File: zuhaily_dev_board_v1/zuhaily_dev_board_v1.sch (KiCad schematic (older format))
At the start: 56 parts, among them J1 USB_B_Micro, J2 Micro_SD_Card, J3 DC_JACK, J4 Conn_01x32_Female, Q1 FS8205A, Q2 FDN340P, SW1 SW_DPDT_x2, SW2 SW_SPST, SW3 SW_DIP_x04, SW4 SW_DIP_x04, SW5 SW_DIP_x04, U1 74LVC245, U10 DW-01, U2 LM1117-5.0, U3 CH340G, U4 LM1117-3.3, U5 ATmega328-PU, U7 TP4056, U8 LMV358, Y1 Crystal_12MHz, Y2 Crystal_16MHz

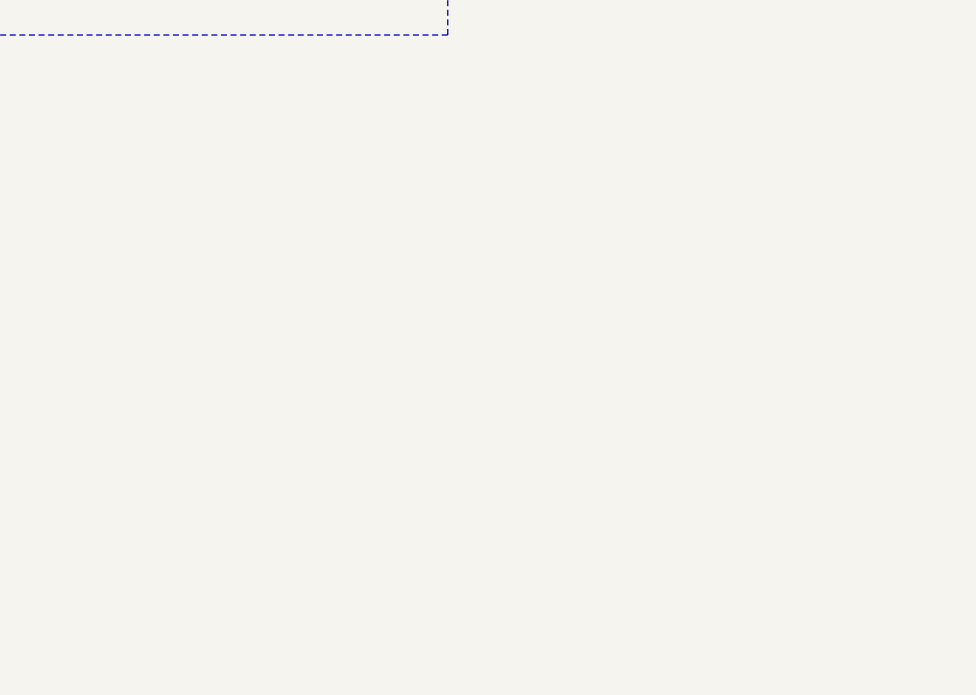
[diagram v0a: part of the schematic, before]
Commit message: added rtc
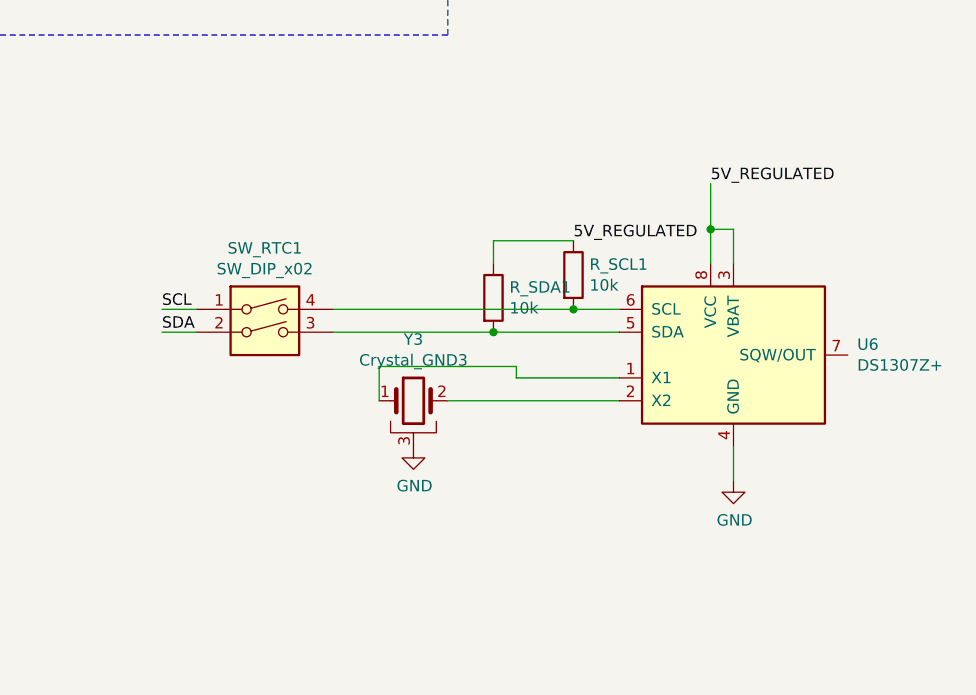
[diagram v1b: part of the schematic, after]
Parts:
- added R_SCL1, R_SDA1: 10k, Resistor_THT:R_Axial_DIN0207_L6.3mm_D2.5mm_P7.62mm_Horizontal, symbol Device:R
- added SW_RTC1: SW_DIP_x02, Button_Switch_THT:SW_DIP_SPSTx02_Slide_9.78x7.26mm_W7.62mm_P2.54mm, symbol Switch:SW_DIP_x02
- added U6: DS1307Z+, Package_SO:SOIC-8_3.9x4.9mm_P1.27mm, symbol Timer_RTC:DS1307Z+
- added Y3: Crystal_GND3, Crystal:Crystal_AT310_D3.0mm_L10.0mm_Horizontal_1EP_style1, symbol Device:Crystal_GND3
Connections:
- net 5V_FILTERED: now also R_SCL1.1, R_SDA1.1, U6.3 (VBAT), U6.8 (VCC)
- net GND: now also U6.4 (GND), Y3.3
- net PC_4: now also SW_RTC1.2
- net PC_5: now also SW_RTC1.1
- new net: U6.1 (X1), Y3.1
- new net: U6.2 (X2), Y3.2
- new net: R_SDA1.2, SW_RTC1.3, U6.5 (SDA)
- new net: R_SCL1.2, SW_RTC1.4, U6.6 (SCL)
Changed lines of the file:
@@
 Wire Wire Line
 	10700 7750 11300 7750
+$Comp
+L Timer_RTC:DS1307Z+ U6
+U 1 1 5C5C03AE
+P 23100 6600
+F 0 "U6" H 23641 6646 50  0000 L CNN
+F 1 "DS1307Z+" H 23641 6555 50  0000 L CNN
+F 2 "Package_SO:SOIC-8_3.9x4.9mm_P1.27mm" H 23100 6100 50  0001 C CNN
+F 3 "https://datasheets.maximintegrated.com/en/ds/DS1307.pdf" H 23100 6600 50  0001 C CNN
+	1    23100 6600
+	1    0    0    -1
+$EndComp
+Text Label 20600 6500 0    50   ~ 0
+SDA
+Text Label 20600 6400 0    50   ~ 0
+SCL
+Text Label 23000 5850 0    50   ~ 0
+5V_REGULATED
+Wire Wire Line
+	23000 6200 23000 6050
+Wire Wire Line
+	23100 6200 23100 6050
+Wire Wire Line
+	23100 6050 23000 6050
+Connection ~ 23000 6050
+Wire Wire Line
+	23000 6050 23000 5850
+Wire Wire Line
+	22600 6700 22150 6700
+Wire Wire Line
+	22150 6700 22150 6650
+$Comp
+L power:GND #PWR0127
+U 1 1 5C665D4A
+P 23100 7150
+F 0 "#PWR0127" H 23100 6900 50  0001 C CNN
+F 1 "GND" H 23105 6977 50  0000 C CNN
+F 2 "" H 23100 7150 50  0001 C CNN
+F 3 "" H 23100 7150 50  0001 C CNN
+	1    23100 7150
+	1    0    0    -1
+$EndComp
+Wire Wire Line
+	23100 7150 23100 7000
+$Comp
+L Device:R R_SCL1
+U 1 1 5C682EB7
+P 22400 6250
+F 0 "R_SCL1" H 22470 6296 50  0000 L CNN
+F 1 "10k" H 22470 6205 50  0000 L CNN
+F 2 "Resistor_THT:R_Axial_DIN0207_L6.3mm_D2.5mm_P7.62mm_Horizontal" V 22330 6250 50  0001 C CNN
+F 3 "~" H 22400 6250 50  0001 C CNN
+	1    22400 6250
+	1    0    0    -1
+$EndComp
+Wire Wire Line
+	22400 6400 22600 6400
+Text Label 22400 6100 0    50   ~ 0
+5V_REGULATED
+$Comp
+L Device:R R_SDA1
+U 1 1 5C697913
+P 22050 6350
+F 0 "R_SDA1" H 22120 6396 50  0000 L CNN
+F 1 "10k" H 22120 6305 50  0000 L CNN
+F 2 "Resistor_THT:R_Axial_DIN0207_L6.3mm_D2.5mm_P7.62mm_Horizontal" V 21980 6350 50  0001 C CNN
+F 3 "~" H 22050 6350 50  0001 C CNN
+	1    22050 6350
+	1    0    0    -1
+$EndComp
+Connection ~ 22050 6500
+Wire Wire Line
+	22050 6200 22050 6100
+Wire Wire Line
+	22050 6100 22400 6100
+Wire Wire Line
+	22050 6500 22600 6500
+Connection ~ 22400 6400
+$Comp
+L Switch:SW_DIP_x02 SW_RTC1
+U 1 1 5C6D7AD0
+P 21050 6500
+F 0 "SW_RTC1" H 21050 6867 50  0000 C CNN
+F 1 "SW_DIP_x02" H 21050 6776 50  0000 C CNN
+F 2 "Button_Switch_THT:SW_DIP_SPSTx02_Slide_9.78x7.26mm_W7.62mm_P2.54mm" H 21050 6500 50  0001 C CNN
+F 3 "" H 21050 6500 50  0001 C CNN
+	1    21050 6500
+	1    0    0    -1
+$EndComp
+Wire Wire Line
+	21350 6400 22400 6400
+Wire Wire Line
+	21350 6500 22050 6500
+Wire Wire Line
+	20750 6400 20600 6400
+Wire Wire Line
+	20750 6500 20600 6500
+$Comp
+L Device:Crystal_GND3 Y3
+U 1 1 5C76D523
+P 21700 6800
+F 0 "Y3" H 21700 7068 50  0000 C CNN
+F 1 "Crystal_GND3" H 21700 6977 50  0000 C CNN
+F 2 "Crystal:Crystal_AT310_D3.0mm_L10.0mm_Horizontal_1EP_style1" H 21700 6800 50  0001 C CNN
+F 3 "~" H 21700 6800 50  0001 C CNN
+	1    21700 6800
+	1    0    0    -1
+$EndComp
+$Comp
+L power:GND #PWR0128
+U 1 1 5C782F61
+P 21700 7000
+F 0 "#PWR0128" H 21700 6750 50  0001 C CNN
+F 1 "GND" H 21705 6827 50  0000 C CNN
+F 2 "" H 21700 7000 50  0001 C CNN
+F 3 "" H 21700 7000 50  0001 C CNN
+	1    21700 7000
+	1    0    0    -1
+$EndComp
+Wire Wire Line
+	21850 6800 22600 6800
+Wire Wire Line
+	21550 6650 21550 6800
+Wire Wire Line
+	21550 6650 22150 6650
 $EndSCHEMATC

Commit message: working version without headers
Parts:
- removed SW4, SW5: SW_DIP_x04, Button_Switch_THT:SW_DIP_SPSTx04_Slide_9.78x12.34mm_W7.62mm_P2.54mm, symbol Switch:SW_DIP_x04
- BT1: symbol Device:Battery_Cell -> zuhaily_dev_board_v1-rescue:Battery_Cell-Device
- C1, C2, C8, C9: symbol c:C -> zuhaily_dev_board_v1-rescue:C-c
- C10, C11, C12, C3, C4, C5, C6, C7: symbol Device:CP_Small -> zuhaily_dev_board_v1-rescue:CP_Small-Device
- D1, D_arduino_rx_led1, D_arduino_tx_led1, D_bat_chrg_led1, D_batt_stdby_led1: symbol Device:LED -> zuhaily_dev_board_v1-rescue:LED-Device
- D2, D3: symbol Device:D -> zuhaily_dev_board_v1-rescue:D-Device
- J1: symbol Connector:USB_B_Micro -> zuhaily_dev_board_v1-rescue:USB_B_Micro-Connector
- J2: symbol Connector:Micro_SD_Card -> zuhaily_dev_board_v1-rescue:Micro_SD_Card-Connector
- J3: symbol tinkerforge:DC_JACK -> zuhaily_dev_board_v1-rescue:DC_JACK-tinkerforge
- J4: symbol Connector:Conn_01x32_Female -> zuhaily_dev_board_v1-rescue:Conn_01x32_Female-Connector
- J_oled_header1: symbol Connector:Conn_01x04_Female -> zuhaily_dev_board_v1-rescue:Conn_01x04_Female-Connector
- Q1: symbol FS8205A:FS8205A -> zuhaily_dev_board_v1-rescue:FS8205A-FS8205A
- Q2: symbol FDN340P:FDN340P -> zuhaily_dev_board_v1-rescue:FDN340P-FDN340P
- R1, R10, R11, R12, R13, R14, R2, R3, R4, R5, R6, R7, R8, R_SCL1, R_SDA1: symbol Device:R -> zuhaily_dev_board_v1-rescue:R-Device
- SW1: symbol Switch:SW_DPDT_x2 -> zuhaily_dev_board_v1-rescue:SW_DPDT_x2-Switch
- SW2: symbol Switch:SW_SPST -> zuhaily_dev_board_v1-rescue:SW_SPST-Switch
- SW3: symbol Switch:SW_DIP_x04 -> zuhaily_dev_board_v1-rescue:SW_DIP_x04-Switch
- SW_RTC1: symbol Switch:SW_DIP_x02 -> zuhaily_dev_board_v1-rescue:SW_DIP_x02-Switch
- U1: symbol tinkerforge:74LVC245 -> zuhaily_dev_board_v1-rescue:74LVC245-tinkerforge
- U10: symbol DW-01:DW-01 -> zuhaily_dev_board_v1-rescue:DW-01-DW-01
- U2: symbol Regulator_Linear:LM1117-5.0 -> zuhaily_dev_board_v1-rescue:LM1117-5.0-Regulator_Linear
- U3: symbol Interface_USB:CH340G -> zuhaily_dev_board_v1-rescue:CH340G-Interface_USB
- U4: symbol Regulator_Linear:LM1117-3.3 -> zuhaily_dev_board_v1-rescue:LM1117-3.3-Regulator_Linear
- U5: symbol MCU_Microchip_ATmega:ATmega328-PU -> zuhaily_dev_board_v1-rescue:ATmega328-PU-MCU_Microchip_ATmega
- U6: symbol Timer_RTC:DS1307Z+ -> zuhaily_dev_board_v1-rescue:DS1307Z+-Timer_RTC
- U7: symbol tp4056:TP4056 -> zuhaily_dev_board_v1-rescue:TP4056-tp4056
- U8: symbol Amplifier_Operational:LMV358 -> zuhaily_dev_board_v1-rescue:LMV358-Amplifier_Operational
- U_ESP1: symbol ESP8266:ESP-01v090 -> zuhaily_dev_board_v1-rescue:ESP-01v090-ESP8266
- Y1, Y2: symbol Device:Crystal -> zuhaily_dev_board_v1-rescue:Crystal-Device
- Y3: symbol Device:Crystal_GND3 -> zuhaily_dev_board_v1-rescue:Crystal_GND3-Device
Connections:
- net 3.3V_REGULATED: now also U_ESP1.7 (VCC)
- net 5V_FILTERED: now also J_oled_header1.4 (Pin_4), Q2.2 (S); no longer Q2.3 (D)
- net ESP_RX: now also U_ESP1.8 (URXD)
- net ESP_TX: now also U_ESP1.1 (UTXD)
- net GND: now also J_oled_header1.3 (Pin_3), U_ESP1.2 (GND)
- net PC_4: now also J_oled_header1.1 (Pin_1)
- net PC_5: now also J_oled_header1.2 (Pin_2)
- net USB_VCC: now also Q2.3 (D); no longer Q2.2 (S)
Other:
- note added: "oled\n\n"
- moved on the sheet: J_oled_header1, R_SCL1, R_SDA1, SW_RTC1, U6, U_ESP1, Y3

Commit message: changed the esp, ds1307 and sd card to header outputs
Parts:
- removed J2: Micro_SD_Card, sd_card_pretty:Conn_uSDcard, symbol zuhaily_dev_board_v1-rescue:Micro_SD_Card-Connector
- removed R_SCL1, R_SDA1: 10k, Resistor_THT:R_Axial_DIN0207_L6.3mm_D2.5mm_P7.62mm_Horizontal, symbol zuhaily_dev_board_v1-rescue:R-Device
- removed SW3: SW_DIP_x04, Button_Switch_THT:SW_DIP_SPSTx04_Slide_9.78x12.34mm_W7.62mm_P2.54mm, symbol zuhaily_dev_board_v1-rescue:SW_DIP_x04-Switch
- removed SW_RTC1: SW_DIP_x02, Button_Switch_THT:SW_DIP_SPSTx02_Slide_9.78x7.26mm_W7.62mm_P2.54mm, symbol zuhaily_dev_board_v1-rescue:SW_DIP_x02-Switch
- removed U1: 74LVC245, Package_SO:SOIC-20W_7.5x12.8mm_P1.27mm, symbol zuhaily_dev_board_v1-rescue:74LVC245-tinkerforge
- removed U6: DS1307Z+, Package_SO:SOIC-8_3.9x4.9mm_P1.27mm, symbol zuhaily_dev_board_v1-rescue:DS1307Z+-Timer_RTC
- removed U_ESP1: ESP-01v090, Connector_PinHeader_2.54mm:PinHeader_2x04_P2.54mm_Vertical, symbol zuhaily_dev_board_v1-rescue:ESP-01v090-ESP8266
- removed Y3: Crystal_GND3, Crystal:Crystal_AT310_D3.0mm_L10.0mm_Horizontal_1EP_style1, symbol zuhaily_dev_board_v1-rescue:Crystal_GND3-Device
- added J?: Conn_01x08_Female, symbol Connector:Conn_01x08_Female
- added J?: Conn_01x04_Female, symbol Connector:Conn_01x04_Female
- added J?: Conn_01x06_Female, symbol Connector:Conn_01x06_Female
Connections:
- net 3.3V_REGULATED: now also J?.1 (Pin_1), J?.2 (Pin_2), J?.2 (Pin_2)
- net ARDUINO_LEVEL_SHIFT_CS: now also J?.6 (Pin_6)
- net ARDUINO_LEVEL_SHIFT_MOSI: now also J?.4 (Pin_4)
- net ARDUINO_LEVEL_SHIFT_SCK: now also J?.5 (Pin_5)
- net ARDUINO_SD_MISO: now also J?.3 (Pin_3)
- net ESP_RX: now also J?.2 (Pin_2)
- net ESP_TX: now also J?.7 (Pin_7)
- net GND: now also J?.1 (Pin_1), J?.1 (Pin_1), J?.8 (Pin_8)
- net PC_4: now also J?.3 (Pin_3)
- net PC_5: now also J?.4 (Pin_4)
- no-connect marks 4 -> 2
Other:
- note added: "DS1307 module\n"
- note added: "Esp 8266\n"
- note added: "sd card module\n"
- note removed: "SD card\n"
- note removed: "esp 8266"
